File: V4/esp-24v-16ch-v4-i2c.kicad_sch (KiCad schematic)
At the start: 12 parts, among them J8 SENSORS, U6 MCP23017_SS, U7 MCP23017_SS, U8 DS2482S-100

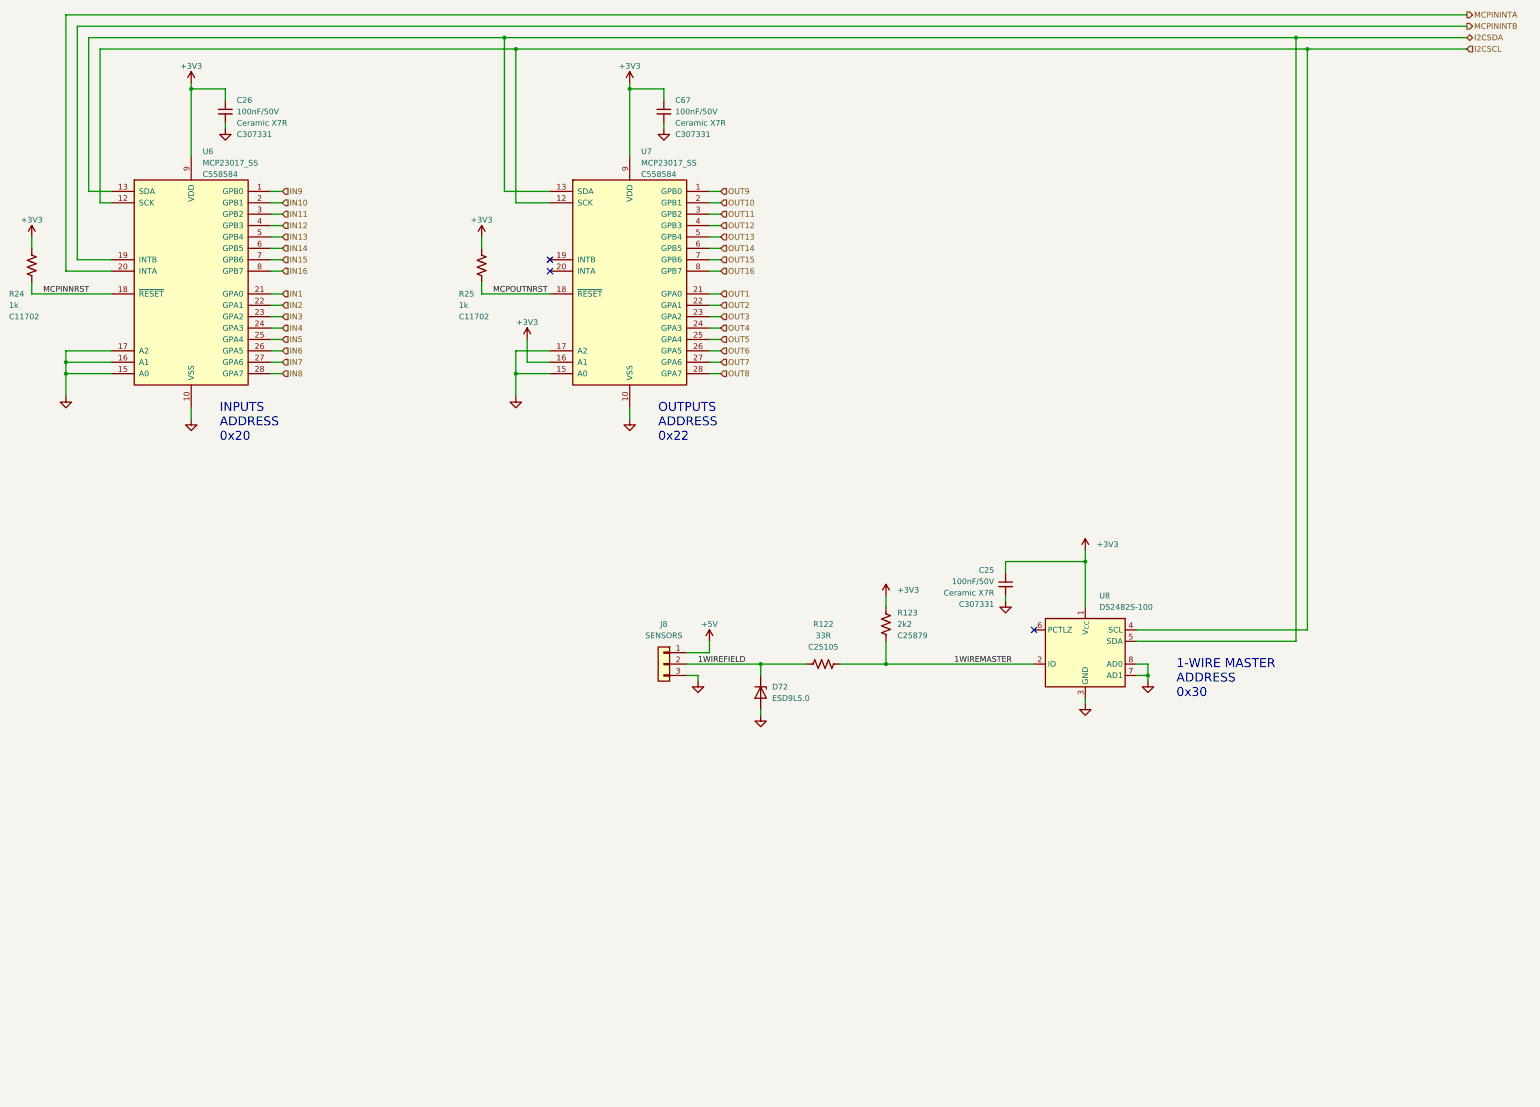
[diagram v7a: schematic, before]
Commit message: Rerouting
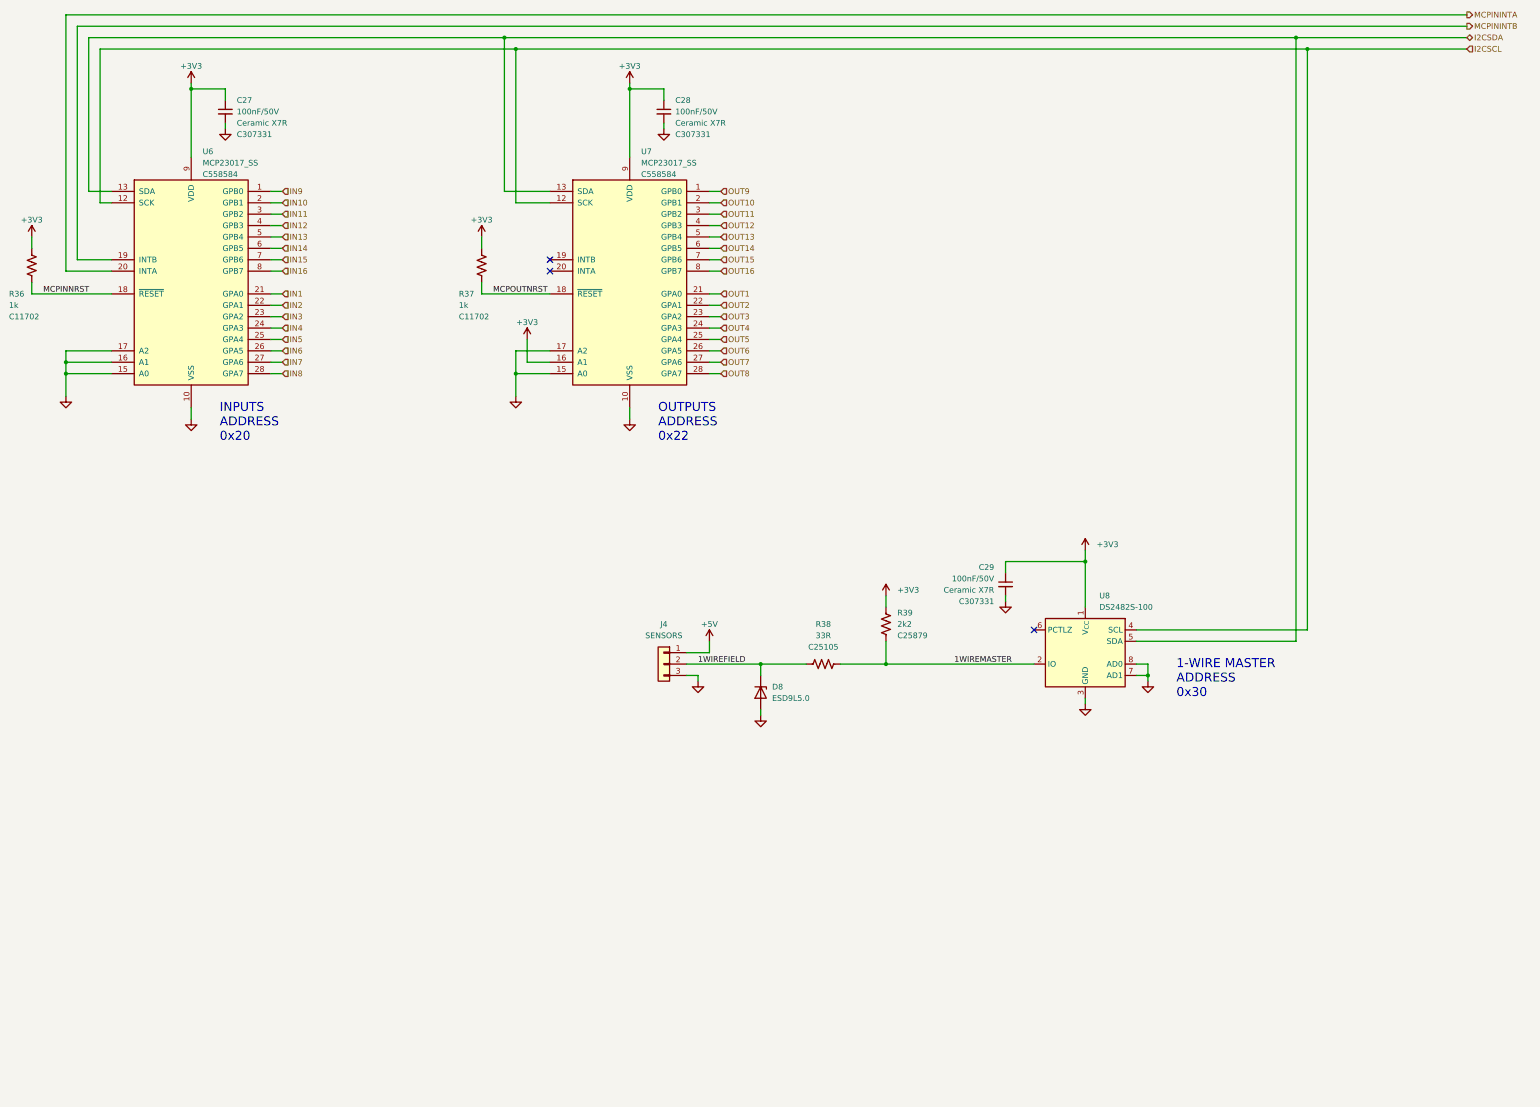
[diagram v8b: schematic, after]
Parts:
- renumbered C26 to C27, C67 to C28, C25 to C29, D72 to D8, J8 to J4, R24 to R36, R25 to R37, R122 to R38, R123 to R39
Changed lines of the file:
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@@
 		(dnp no)
 		(fields_autoplaced yes)
-		(property "Reference" "#PWR074"
+		(property "Reference" "#PWR0244"
 			(at 158.75 115.57 0)
 			(effects
@@
 			(project "esp-24v-16ch-v4"
 				(path "/2bc5a21a-1d79-419d-a592-6852cc07b00a/8d06b51d-d00b-4f80-9ffb-ab0131290cf2"
-					(reference "#PWR074")
+					(reference "#PWR0244")
 					(unit 1)
 				)
@@
 		(dnp no)
 		(fields_autoplaced yes)
-		(property "Reference" "#PWR0244"
+		(property "Reference" "#PWR0238"
 			(at 93.98 55.88 0)
 			(effects
@@
 			(project "esp-24v-16ch-v4"
 				(path "/2bc5a21a-1d79-419d-a592-6852cc07b00a/8d06b51d-d00b-4f80-9ffb-ab0131290cf2"
-					(reference "#PWR0244")
+					(reference "#PWR0238")
 					(unit 1)
 				)
@@
 		(on_board yes)
 		(dnp no)
-		(property "Reference" "#PWR079"
+		(property "Reference" "#PWR0243"
 			(at 184.15 43.18 0)
 			(effects
@@
 			(project "esp-24v-16ch-v4"
 				(path "/2bc5a21a-1d79-419d-a592-6852cc07b00a/8d06b51d-d00b-4f80-9ffb-ab0131290cf2"
-					(reference "#PWR079")
+					(reference "#PWR0243")
 					(unit 1)
 				)
@@
 		(dnp no)
 		(fields_autoplaced yes)
-		(property "Reference" "J8"
+		(property "Reference" "J4"
 			(at 191.77 160.02 0)
 			(effects
@@
 			(project "esp-24v-16ch-v4"
 				(path "/2bc5a21a-1d79-419d-a592-6852cc07b00a/8d06b51d-d00b-4f80-9ffb-ab0131290cf2"
-					(reference "J8")
+					(reference "J4")
 					(unit 1)
 				)
@@
 		(dnp no)
 		(fields_autoplaced yes)
-		(property "Reference" "R122"
+		(property "Reference" "R38"
 			(at 227.33 160.02 90)
 			(effects
@@
 			(project "esp-24v-16ch-v4"
 				(path "/2bc5a21a-1d79-419d-a592-6852cc07b00a/8d06b51d-d00b-4f80-9ffb-ab0131290cf2"
-					(reference "R122")
+					(reference "R38")
 					(unit 1)
 				)
@@
 		(dnp no)
 		(fields_autoplaced yes)
-		(property "Reference" "#PWR077"
+		(property "Reference" "#PWR0229"
 			(at 285.75 184.15 0)
 			(effects
@@
 			(project "esp-24v-16ch-v4"
 				(path "/2bc5a21a-1d79-419d-a592-6852cc07b00a/8d06b51d-d00b-4f80-9ffb-ab0131290cf2"
-					(reference "#PWR077")
+					(reference "#PWR0229")
 					(unit 1)
 				)
@@
 		(dnp no)
 		(fields_autoplaced yes)
-		(property "Reference" "#PWR0245"
+		(property "Reference" "#PWR0241"
 			(at 191.77 55.88 0)
 			(effects
@@
 			(project "esp-24v-16ch-v4"
 				(path "/2bc5a21a-1d79-419d-a592-6852cc07b00a/8d06b51d-d00b-4f80-9ffb-ab0131290cf2"
-					(reference "#PWR0245")
+					(reference "#PWR0241")
 					(unit 1)
 				)
@@
 		(on_board yes)
 		(dnp no)
-		(property "Reference" "R24"
+		(property "Reference" "R36"
 			(at 45.72 86.36 0)
 			(effects
@@
 			(project "esp-24v-16ch-v4"
 				(path "/2bc5a21a-1d79-419d-a592-6852cc07b00a/8d06b51d-d00b-4f80-9ffb-ab0131290cf2"
-					(reference "R24")
+					(reference "R36")
 					(unit 1)
 				)
@@
 		(dnp no)
 		(fields_autoplaced yes)
-		(property "Reference" "#PWR076"
+		(property "Reference" "#PWR0247"
 			(at 285.75 147.32 0)
 			(effects
@@
 			(project ""
 				(path "/2bc5a21a-1d79-419d-a592-6852cc07b00a/8d06b51d-d00b-4f80-9ffb-ab0131290cf2"
-					(reference "#PWR076")
+					(reference "#PWR0247")
 					(unit 1)
 				)
@@
 		(on_board yes)
 		(dnp no)
-		(property "Reference" "R123"
+		(property "Reference" "R39"
 			(at 243.84 157.48 0)
 			(effects
@@
 			(project "esp-24v-16ch-v4"
 				(path "/2bc5a21a-1d79-419d-a592-6852cc07b00a/8d06b51d-d00b-4f80-9ffb-ab0131290cf2"
-					(reference "R123")
+					(reference "R39")
 					(unit 1)
 				)
@@
 		(on_board yes)
 		(dnp no)
-		(property "Reference" "C26"
+		(property "Reference" "C27"
 			(at 96.52 43.18 0)
 			(effects
@@
 			(project "esp-24v-16ch-v4"
 				(path "/2bc5a21a-1d79-419d-a592-6852cc07b00a/8d06b51d-d00b-4f80-9ffb-ab0131290cf2"
-					(reference "C26")
+					(reference "C27")
 					(unit 1)
 				)
@@
 		(dnp no)
 		(fields_autoplaced yes)
-		(property "Reference" "#PWR072"
+		(property "Reference" "#PWR0234"
 			(at 267.97 161.29 0)
 			(effects
@@
 			(project "esp-24v-16ch-v4"
 				(path "/2bc5a21a-1d79-419d-a592-6852cc07b00a/8d06b51d-d00b-4f80-9ffb-ab0131290cf2"
-					(reference "#PWR072")
+					(reference "#PWR0234")
 					(unit 1)
 				)
@@
 		(dnp no)
 		(fields_autoplaced yes)
-		(property "Reference" "#PWR067"
+		(property "Reference" "#PWR0237"
 			(at 58.42 115.57 0)
 			(effects
@@
 			(project "esp-24v-16ch-v4"
 				(path "/2bc5a21a-1d79-419d-a592-6852cc07b00a/8d06b51d-d00b-4f80-9ffb-ab0131290cf2"
-					(reference "#PWR067")
+					(reference "#PWR0237")
 					(unit 1)
 				)
@@
 		(dnp no)
 		(fields_autoplaced yes)
-		(property "Reference" "#PWR069"
+		(property "Reference" "#PWR0232"
 			(at 199.39 179.07 0)
 			(effects
@@
 			(project "esp-24v-16ch-v4"
 				(path "/2bc5a21a-1d79-419d-a592-6852cc07b00a/8d06b51d-d00b-4f80-9ffb-ab0131290cf2"
-					(reference "#PWR069")
+					(reference "#PWR0232")
 					(unit 1)
 				)
@@
 		(dnp no)
 		(fields_autoplaced yes)
-		(property "Reference" "C25"
-			(at 265.43 147.9613 0)
+		(property "Reference" "C29"
+			(at 265.43 147.3262 0)
 			(effects
 				(font
@@
 		)
 		(property "Value" "100nF/50V"
-			(at 265.43 150.5013 0)
+			(at 265.43 149.8662 0)
 			(effects
 				(font
@@
 		)
 		(property "Technology" "Ceramic X7R"
-			(at 265.43 153.0413 0)
+			(at 265.43 152.4062 0)
 			(effects
 				(font
@@
 		)
 		(property "LCSC Part #" "C307331"
-			(at 265.43 155.5813 0)
+			(at 265.43 154.9462 0)
 			(effects
 				(font
@@
 			(project "esp-24v-16ch-v4"
 				(path "/2bc5a21a-1d79-419d-a592-6852cc07b00a/8d06b51d-d00b-4f80-9ffb-ab0131290cf2"
-					(reference "C25")
+					(reference "C29")
 					(unit 1)
 				)
@@
 		(dnp no)
 		(fields_autoplaced yes)
-		(property "Reference" "#PWR078"
+		(property "Reference" "#PWR0246"
 			(at 299.72 179.07 0)
 			(effects
@@
 			(project "esp-24v-16ch-v4"
 				(path "/2bc5a21a-1d79-419d-a592-6852cc07b00a/8d06b51d-d00b-4f80-9ffb-ab0131290cf2"
-					(reference "#PWR078")
+					(reference "#PWR0246")
 					(unit 1)
 				)
@@
 		(dnp no)
 		(fields_autoplaced yes)
-		(property "Reference" "#PWR082"
+		(property "Reference" "#PWR0230"
 			(at 213.36 186.69 0)
 			(effects
@@
 			(project "esp-24v-16ch-v4"
 				(path "/2bc5a21a-1d79-419d-a592-6852cc07b00a/8d06b51d-d00b-4f80-9ffb-ab0131290cf2"
-					(reference "#PWR082")
+					(reference "#PWR0230")
 					(unit 1)
 				)
@@
 		(on_board yes)
 		(dnp no)
-		(property "Reference" "#PWR073"
+		(property "Reference" "#PWR0235"
 			(at 151.13 77.47 0)
 			(effects
@@
 			(project "esp-24v-16ch-v4"
 				(path "/2bc5a21a-1d79-419d-a592-6852cc07b00a/8d06b51d-d00b-4f80-9ffb-ab0131290cf2"
-					(reference "#PWR073")
+					(reference "#PWR0235")
 					(unit 1)
 				)
@@
 		(on_board yes)
 		(dnp no)
-		(property "Reference" "#PWR075"
+		(property "Reference" "#PWR0245"
 			(at 161.29 100.33 0)
 			(effects
@@
 			(project "esp-24v-16ch-v4"
 				(path "/2bc5a21a-1d79-419d-a592-6852cc07b00a/8d06b51d-d00b-4f80-9ffb-ab0131290cf2"
-					(reference "#PWR075")
+					(reference "#PWR0245")
 					(unit 1)
 				)
@@
 		(on_board yes)
 		(dnp no)
-		(property "Reference" "#PWR068"
+		(property "Reference" "#PWR0231"
 			(at 201.93 167.64 0)
 			(effects
@@
 			(project "esp-24v-16ch-v4"
 				(path "/2bc5a21a-1d79-419d-a592-6852cc07b00a/8d06b51d-d00b-4f80-9ffb-ab0131290cf2"
-					(reference "#PWR068")
+					(reference "#PWR0231")
 					(unit 1)
 				)
@@
 		(on_board yes)
 		(dnp no)
-		(property "Reference" "#PWR066"
+		(property "Reference" "#PWR0240"
 			(at 50.8 77.47 0)
 			(effects
@@
 			(project "esp-24v-16ch-v4"
 				(path "/2bc5a21a-1d79-419d-a592-6852cc07b00a/8d06b51d-d00b-4f80-9ffb-ab0131290cf2"
-					(reference "#PWR066")
+					(reference "#PWR0240")
 					(unit 1)
 				)
@@
 		(dnp no)
 		(fields_autoplaced yes)
-		(property "Reference" "#PWR071"
+		(property "Reference" "#PWR0236"
 			(at 86.36 120.65 0)
 			(effects
@@
 			(project "esp-24v-16ch-v4"
 				(path "/2bc5a21a-1d79-419d-a592-6852cc07b00a/8d06b51d-d00b-4f80-9ffb-ab0131290cf2"
-					(reference "#PWR071")
+					(reference "#PWR0236")
 					(unit 1)
 				)
@@
 		(dnp no)
 		(fields_autoplaced yes)
-		(property "Reference" "#PWR080"
+		(property "Reference" "#PWR0242"
 			(at 184.15 120.65 0)
 			(effects
@@
 			(project "esp-24v-16ch-v4"
 				(path "/2bc5a21a-1d79-419d-a592-6852cc07b00a/8d06b51d-d00b-4f80-9ffb-ab0131290cf2"
-					(reference "#PWR080")
+					(reference "#PWR0242")
 					(unit 1)
 				)
@@
 		(dnp no)
 		(fields_autoplaced yes)
-		(property "Reference" "D72"
+		(property "Reference" "D8"
 			(at 215.9 173.9899 90)
 			(effects
@@
 			(project ""
 				(path "/2bc5a21a-1d79-419d-a592-6852cc07b00a/8d06b51d-d00b-4f80-9ffb-ab0131290cf2"
-					(reference "D72")
+					(reference "D8")
 					(unit 1)
 				)
@@
 		(on_board yes)
 		(dnp no)
-		(property "Reference" "R25"
+		(property "Reference" "R37"
 			(at 146.05 86.36 0)
 			(effects
@@
 			(project "esp-24v-16ch-v4"
 				(path "/2bc5a21a-1d79-419d-a592-6852cc07b00a/8d06b51d-d00b-4f80-9ffb-ab0131290cf2"
-					(reference "R25")
+					(reference "R37")
 					(unit 1)
 				)
@@
 		(on_board yes)
 		(dnp no)
-		(property "Reference" "C67"
+		(property "Reference" "C28"
 			(at 194.31 43.18 0)
 			(effects
@@
 			(project "esp-24v-16ch-v4"
 				(path "/2bc5a21a-1d79-419d-a592-6852cc07b00a/8d06b51d-d00b-4f80-9ffb-ab0131290cf2"
-					(reference "C67")
+					(reference "C28")
 					(unit 1)
 				)
@@
 		(on_board yes)
 		(dnp no)
-		(property "Reference" "#PWR070"
+		(property "Reference" "#PWR0239"
 			(at 86.36 43.18 0)
 			(effects
@@
 			(project "esp-24v-16ch-v4"
 				(path "/2bc5a21a-1d79-419d-a592-6852cc07b00a/8d06b51d-d00b-4f80-9ffb-ab0131290cf2"
-					(reference "#PWR070")
+					(reference "#PWR0239")
 					(unit 1)
 				)
@@
 		(dnp no)
 		(fields_autoplaced yes)
-		(property "Reference" "#PWR081"
+		(property "Reference" "#PWR0233"
 			(at 241.3 157.48 0)
 			(effects
@@
 			(project "esp-24v-16ch-v4"
 				(path "/2bc5a21a-1d79-419d-a592-6852cc07b00a/8d06b51d-d00b-4f80-9ffb-ab0131290cf2"
-					(reference "#PWR081")
-					(unit 1)
-				)
+					(reference "#PWR0233")
+					(unit 1)
+				)
